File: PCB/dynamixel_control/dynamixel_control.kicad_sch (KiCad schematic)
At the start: 34 parts, among them J1 12V, J2 RS232, J3 5V, J4 3.3V, J5 I2C, Q1 SSM3J372R, SW1 LIMIT_SWITCH, U1 R-78E5.0-0.5, U2 SN74AHC1G14, U3 LM810M3-4.63, U4 Teensy_4.0, U5 MAX3221E, U6 ICM-40627

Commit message: Fix issues. Add schematic files.
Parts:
- added C6: 10nF/25V, Capacitor_SMD:C_0805_2012Metric, symbol Device:C
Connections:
- net +3.3V: now also C6.1
- net GND: now also C6.2
- net IMU_INT1: now also U4.14 (14/A0/TX3/SPDIF_OUT/PWM); no longer U4.13 (13/LED/SCK/PWM)
- net IMU_INT2: now also U4.15 (15/A1/RX3/SPDIF_IN/PWM); no longer U4.16 (16/A2/RX4/SCL1)
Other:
- note added: "I2C Address 1101000: R9=NI, R10=0 1101001: R9=0, R10=NI NI: Not Installed"
- title: (none) -> Dynamixel Control
- moved on the sheet: C12, C13

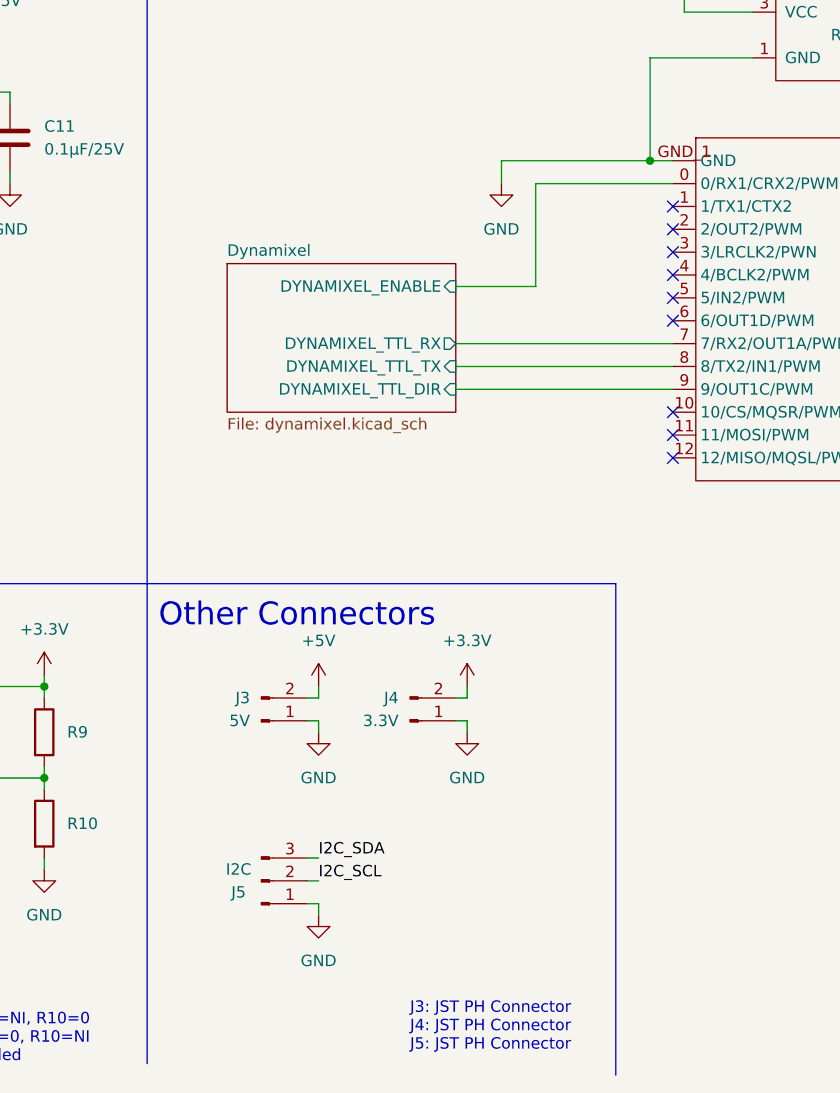
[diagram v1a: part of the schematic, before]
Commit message: Add Debug UART connector to dynamixel_control.
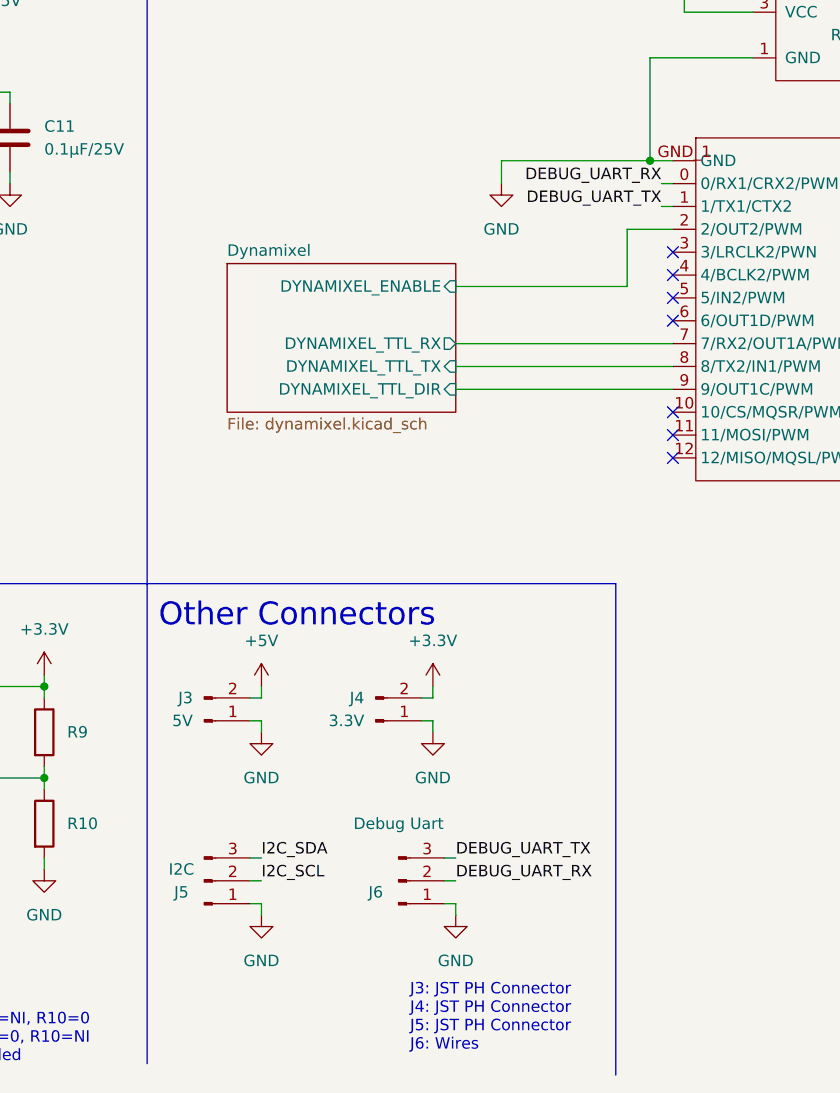
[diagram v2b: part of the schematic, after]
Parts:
- added J6: Debug Uart, Connector_PinHeader_1.00mm:PinHeader_1x03_P1.00mm_Vertical, symbol Connector:Conn_01x03_Male
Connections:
- net Dynamixel/DYNAMIXEL_ENABLE: now also U4.2 (2/OUT2/PWM); no longer U4.0 (0/RX1/CRX2/PWM)
- net GND: now also J6.1 (Pin_1)
- net DEBUG_UART_TX: now reaches U4.1 (1/TX1/CTX2)
- net DEBUG_UART_TX: now also J6.3 (Pin_3)
- new net DEBUG_UART_RX: J6.2 (Pin_2), U4.0 (0/RX1/CRX2/PWM)
- no-connect marks 13 -> 11
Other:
- note added: "J3: JST PH Connector J4: JST PH Connector J5: JST PH Connector J6: Wires"
- note removed: "J3: JST PH Connector J4: JST PH Connector J5: JST PH Connector"
- moved on the sheet: J3, J4, J5

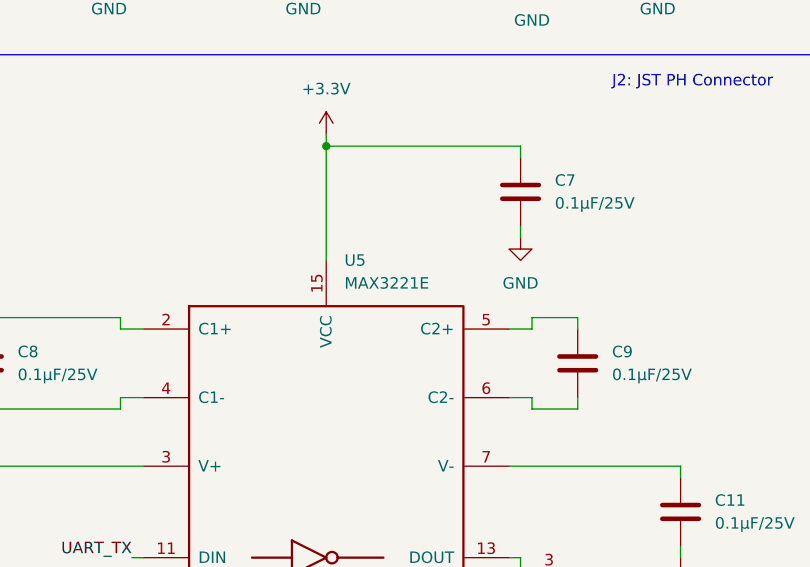
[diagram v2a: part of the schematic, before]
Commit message: Change MAX3221E by SN65C3221E.
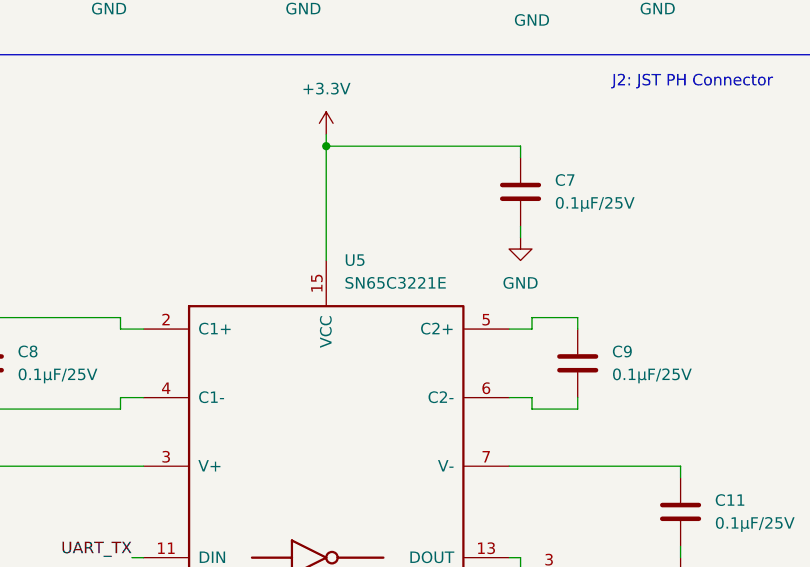
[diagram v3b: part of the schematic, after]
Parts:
- removed U5: MAX3221E, Package_SO:TSSOP-16_4.4x5mm_P0.65mm, symbol t-top:MAX3221E
- added U5: SN65C3221E, Package_SO:TSSOP-16_4.4x5mm_P0.65mm, symbol t-top:SN65C3221E
- J6: footprint Connector_PinHeader_1.00mm:PinHeader_1x03_P1.00mm_Vertical -> Connector_PinHeader_1.27mm:PinHeader_1x03_P1.27mm_Vertical
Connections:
- net +3.3V: now also U5.12 (FORCEON), U5.15 (VCC), U5.16 (~{FORCEOFF})
- net GND: now also U5.1 (~{EN}), U5.14 (GND)
- net UART_RX: now also U5.9 (ROUT)
- net UART_TX: now also U5.11 (DIN)
- net ~{RS232_INVALID}: now also U5.10 (~{INVALID})
- net at C8.1: now also U5.2 (C1+)
- net at C8.2: now also U5.4 (C1-)
- net at J2.2 (Pin_2): now also U5.8 (RIN)
- net at J2.3 (Pin_3): now also U5.13 (DOUT)
- net at C11.1: now also U5.7 (V-)
- net at C10.1: now also U5.3 (V+)
- net at C9.1: now also U5.5 (C2+)
- net at C9.2: now also U5.6 (C2-)
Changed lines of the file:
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@@
     (property "Reference" "J6" (id 0) (at 149.86 177.8 0))
     (property "Value" "Debug Uart" (id 1) (at 152.4 170.18 0))
-    (property "Footprint" "Connector_PinHeader_1.00mm:PinHeader_1x03_P1.00mm_Vertical" (id 2) (at 152.4 176.53 0)
+    (property "Footprint" "Connector_PinHeader_1.27mm:PinHeader_1x03_P1.27mm_Vertical" (id 2) (at 152.4 176.53 0)
       (effects (font (size 1.27 1.27)) hide)
     )
@@
     (pin "3")
   )
-  (symbol (lib_id "power:GND") (at 179.07 50.8 0) (unit 1)
-    (in_bom yes) (on_board yes) (fields_autoplaced)
-    (property "Reference" "#PWR0135" (id 0) (at 179.07 57.15 0)
-      (effects (font (size 1.27 1.27)) hide)
-    )
-    (property "Value" "GND" (id 1) (at 179.07 55.88 0))
-    (property "Footprint" "" (id 2) (at 179.07 50.8 0)
-      (effects (font (size 1.27 1.27)) hide)
-    )
-    (property "Datasheet" "" (id 3) (at 179.07 50.8 0)
-      (effects (font (size 1.27 1.27)) hide)
-    )
-    (pin "1")
-  )
-  (symbol (lib_id "Device:C") (at 109.22 93.98 0) (unit 1)
-    (in_bom yes) (on_board yes) (fields_autoplaced)
-    (property "Reference" "C11" (id 0) (at 113.03 92.7099 0)
-      (effects (font (size 1.27 1.27)) (justify left))
-    )
-    (property "Value" "0.1µF/25V" (id 1) (at 113.03 95.2499 0)
-      (effects (font (size 1.27 1.27)) (justify left))
-    )
-    (property "Footprint" "Capacitor_SMD:C_0805_2012Metric" (id 2) (at 110.1852 97.79 0)
-      (effects (font (size 1.27 1.27)) hide)
-    )
-    (property "Datasheet" "~" (id 3) (at 109.22 93.98 0)
-      (effects (font (size 1.27 1.27)) hide)
-    )
-    (pin "1")
-    (pin "2")
-  )
-  (symbol (lib_id "Connector:Conn_01x03_Male") (at 130.81 176.53 0) (mirror x) (unit 1)
-    (in_bom yes) (on_board yes)
-    (property "Reference" "J5" (id 0) (at 128.27 177.8 0))
-    (property "Value" "I2C" (id 1) (at 128.27 175.26 0))
-    (property "Footprint" "Connector_JST:JST_PH_B3B-PH-K_1x03_P2.00mm_Vertical" (id 2) (at 130.81 176.53 0)
-      (effects (font (size 1.27 1.27)) hide)
-    )
-    (property "Datasheet" "~" (id 3) (at 130.81 176.53 0)
-      (effects (font (size 1.27 1.27)) hide)
-    )
-    (pin "1")
-    (pin "2")
-    (pin "3")
-  )
-  (symbol (lib_id "power:GND") (at 67.31 33.02 0) (unit 1)
-    (in_bom yes) (on_board yes) (fields_autoplaced)
-    (property "Reference" "#PWR0113" (id 0) (at 67.31 39.37 0)
-      (effects (font (size 1.27 1.27)) hide)
-    )
-    (property "Value" "GND" (id 1) (at 67.31 38.1 0))
-    (property "Footprint" "" (id 2) (at 67.31 33.02 0)
-      (effects (font (size 1.27 1.27)) hide)
-    )
-    (property "Datasheet" "" (id 3) (at 67.31 33.02 0)
-      (effects (font (size 1.27 1.27)) hide)
-    )
-    (pin "1")
-  )
-  (symbol (lib_id "Switch:SW_SPST") (at 132.08 43.18 90) (unit 1)
-    (in_bom yes) (on_board yes)
-    (property "Reference" "SW1" (id 0) (at 133.35 41.9099 90)
-      (effects (font (size 1.27 1.27)) (justify right))
-    )
-    (property "Value" "LIMIT_SWITCH" (id 1) (at 133.35 44.45 90)
-      (effects (font (size 1.27 1.27)) (justify right))
-    )
-    (property "Footprint" "Connector_JST:JST_PH_B2B-PH-K_1x02_P2.00mm_Vertical" (id 2) (at 132.08 43.18 0)
-      (effects (font (size 1.27 1.27)) hide)
-    )
-    (property "Datasheet" "~" (id 3) (at 132.08 43.18 0)
-      (effects (font (size 1.27 1.27)) hide)
-    )
-    (pin "1")
-    (pin "2")
-  )
-  (symbol (lib_id "Device:C") (at 16.51 93.98 0) (unit 1)
-    (in_bom yes) (on_board yes) (fields_autoplaced)
-    (property "Reference" "C10" (id 0) (at 20.32 92.7099 0)
-      (effects (font (size 1.27 1.27)) (justify left))
-    )
-    (property "Value" "0.1µF/25V" (id 1) (at 20.32 95.2499 0)
-      (effects (font (size 1.27 1.27)) (justify left))
-    )
-    (property "Footprint" "Capacitor_SMD:C_0805_2012Metric" (id 2) (at 17.4752 97.79 0)
-      (effects (font (size 1.27 1.27)) hide)
-    )
-    (property "Datasheet" "~" (id 3) (at 16.51 93.98 0)
-      (effects (font (size 1.27 1.27)) hide)
-    )
-    (pin "1")
-    (pin "2")
-  )
-  (symbol (lib_id "t-top:MAX3221E") (at 69.85 96.52 0) (unit 1)
+  (symbol (lib_id "t-top:SN65C3221E") (at 69.85 96.52 0) (unit 1)
     (in_bom yes) (on_board yes) (fields_autoplaced)
     (property "Reference" "U5" (id 0) (at 71.8694 66.04 0)
       (effects (font (size 1.27 1.27)) (justify left))
     )
-    (property "Value" "MAX3221E" (id 1) (at 71.8694 68.58 0)
+    (property "Value" "SN65C3221E" (id 1) (at 71.8694 68.58 0)
       (effects (font (size 1.27 1.27)) (justify left))
     )
@@
     (pin "8")
     (pin "9")
+  )
+  (symbol (lib_id "power:GND") (at 179.07 50.8 0) (unit 1)
+    (in_bom yes) (on_board yes) (fields_autoplaced)
+    (property "Reference" "#PWR0135" (id 0) (at 179.07 57.15 0)
+      (effects (font (size 1.27 1.27)) hide)
+    )
+    (property "Value" "GND" (id 1) (at 179.07 55.88 0))
+    (property "Footprint" "" (id 2) (at 179.07 50.8 0)
+      (effects (font (size 1.27 1.27)) hide)
+    )
+    (property "Datasheet" "" (id 3) (at 179.07 50.8 0)
+      (effects (font (size 1.27 1.27)) hide)
+    )
+    (pin "1")
+  )
+  (symbol (lib_id "Device:C") (at 109.22 93.98 0) (unit 1)
+    (in_bom yes) (on_board yes) (fields_autoplaced)
+    (property "Reference" "C11" (id 0) (at 113.03 92.7099 0)
+      (effects (font (size 1.27 1.27)) (justify left))
+    )
+    (property "Value" "0.1µF/25V" (id 1) (at 113.03 95.2499 0)
+      (effects (font (size 1.27 1.27)) (justify left))
+    )
+    (property "Footprint" "Capacitor_SMD:C_0805_2012Metric" (id 2) (at 110.1852 97.79 0)
+      (effects (font (size 1.27 1.27)) hide)
+    )
+    (property "Datasheet" "~" (id 3) (at 109.22 93.98 0)
+      (effects (font (size 1.27 1.27)) hide)
+    )
+    (pin "1")
+    (pin "2")
+  )
+  (symbol (lib_id "Connector:Conn_01x03_Male") (at 130.81 176.53 0) (mirror x) (unit 1)
+    (in_bom yes) (on_board yes)
+    (property "Reference" "J5" (id 0) (at 128.27 177.8 0))
+    (property "Value" "I2C" (id 1) (at 128.27 175.26 0))
+    (property "Footprint" "Connector_JST:JST_PH_B3B-PH-K_1x03_P2.00mm_Vertical" (id 2) (at 130.81 176.53 0)
+      (effects (font (size 1.27 1.27)) hide)
+    )
+    (property "Datasheet" "~" (id 3) (at 130.81 176.53 0)
+      (effects (font (size 1.27 1.27)) hide)
+    )
+    (pin "1")
+    (pin "2")
+    (pin "3")
+  )
+  (symbol (lib_id "power:GND") (at 67.31 33.02 0) (unit 1)
+    (in_bom yes) (on_board yes) (fields_autoplaced)
+    (property "Reference" "#PWR0113" (id 0) (at 67.31 39.37 0)
+      (effects (font (size 1.27 1.27)) hide)
+    )
+    (property "Value" "GND" (id 1) (at 67.31 38.1 0))
+    (property "Footprint" "" (id 2) (at 67.31 33.02 0)
+      (effects (font (size 1.27 1.27)) hide)
+    )
+    (property "Datasheet" "" (id 3) (at 67.31 33.02 0)
+      (effects (font (size 1.27 1.27)) hide)
+    )
+    (pin "1")
+  )
+  (symbol (lib_id "Switch:SW_SPST") (at 132.08 43.18 90) (unit 1)
+    (in_bom yes) (on_board yes)
+    (property "Reference" "SW1" (id 0) (at 133.35 41.9099 90)
+      (effects (font (size 1.27 1.27)) (justify right))
+    )
+    (property "Value" "LIMIT_SWITCH" (id 1) (at 133.35 44.45 90)
+      (effects (font (size 1.27 1.27)) (justify right))
+    )
+    (property "Footprint" "Connector_JST:JST_PH_B2B-PH-K_1x02_P2.00mm_Vertical" (id 2) (at 132.08 43.18 0)
+      (effects (font (size 1.27 1.27)) hide)
+    )
+    (property "Datasheet" "~" (id 3) (at 132.08 43.18 0)
+      (effects (font (size 1.27 1.27)) hide)
+    )
+    (pin "1")
+    (pin "2")
+  )
+  (symbol (lib_id "Device:C") (at 16.51 93.98 0) (unit 1)
+    (in_bom yes) (on_board yes) (fields_autoplaced)
+    (property "Reference" "C10" (id 0) (at 20.32 92.7099 0)
+      (effects (font (size 1.27 1.27)) (justify left))
+    )
+    (property "Value" "0.1µF/25V" (id 1) (at 20.32 95.2499 0)
+      (effects (font (size 1.27 1.27)) (justify left))
+    )
+    (property "Footprint" "Capacitor_SMD:C_0805_2012Metric" (id 2) (at 17.4752 97.79 0)
+      (effects (font (size 1.27 1.27)) hide)
+    )
+    (property "Datasheet" "~" (id 3) (at 16.51 93.98 0)
+      (effects (font (size 1.27 1.27)) hide)
+    )
+    (pin "1")
+    (pin "2")
   )
   (symbol (lib_id "power:GND") (at 52.07 185.42 0) (unit 1)
@@
     )
     (path "/10b4d070-9fcb-4662-96ad-09ebfc6675de"
-      (reference "J6") (unit 1) (value "Debug Uart") (footprint "Connector_PinHeader_1.00mm:PinHeader_1x03_P1.00mm_Vertical")
+      (reference "J6") (unit 1) (value "Debug Uart") (footprint "Connector_PinHeader_1.27mm:PinHeader_1x03_P1.27mm_Vertical")
     )
     (path "/d35e0dd5-65a6-42a8-88be-82a5f6d1ca91/a88625c8-ea46-49fd-853f-e88ba2b2fda3"
@@
       (reference "U4") (unit 1) (value "Teensy_4.0") (footprint "t-top:Teensy_4.0")
     )
-    (path "/c0ae8657-d6e0-4e58-ba13-3af268c90837"
-      (reference "U5") (unit 1) (value "MAX3221E") (footprint "Package_SO:TSSOP-16_4.4x5mm_P0.65mm")
+    (path "/abc9de71-4b88-443a-8b78-70ae89426f7f"
+      (reference "U5") (unit 1) (value "SN65C3221E") (footprint "Package_SO:TSSOP-16_4.4x5mm_P0.65mm")
     )
     (path "/7d19cc23-7b93-4a41-844a-abd34722bd1b"

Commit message: Fix PCBs.
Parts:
- removed J3: 5V, Connector_JST:JST_PH_B2B-PH-K_1x02_P2.00mm_Vertical, symbol Connector:Conn_01x02_Male
- removed J4: 3.3V, Connector_JST:JST_PH_B2B-PH-K_1x02_P2.00mm_Vertical, symbol Connector:Conn_01x02_Male
- removed J5: I2C, Connector_JST:JST_PH_B3B-PH-K_1x03_P2.00mm_Vertical, symbol Connector:Conn_01x03_Male
- added C14: 10µF/25V, Capacitor_SMD:C_0805_2012Metric, symbol Device:C
- added L2: 12µH (RLS-126), Inductor_SMD:L_1812_4532Metric, symbol Device:L
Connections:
- net +5V: now also C14.1, L2.2; no longer C3.1, U1.3 (VOUT)
- net GND: now also C14.2
- new net: C3.1, L2.1, U1.3 (VOUT)
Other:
- note added: "Debug UART"
- note added: "J6: Wires"
- note removed: "J3: JST PH Connector J4: JST PH Connector J5: JST PH Connector J6: Wires"
- note removed: "Other Connectors"
- moved on the sheet: C1, C2, C3, J1, J6, L1, U1

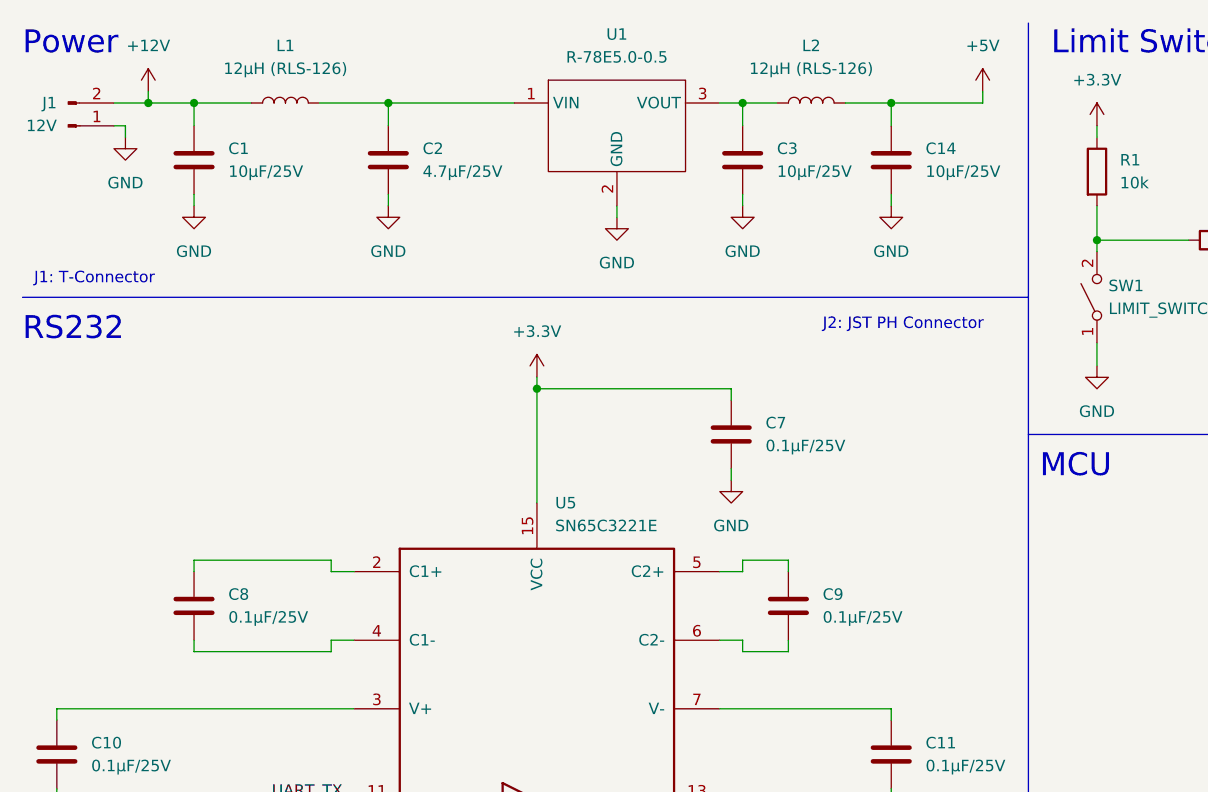
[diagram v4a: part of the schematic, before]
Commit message: Add a PI filter to buck_boost. Fix ringing for other PI filters.
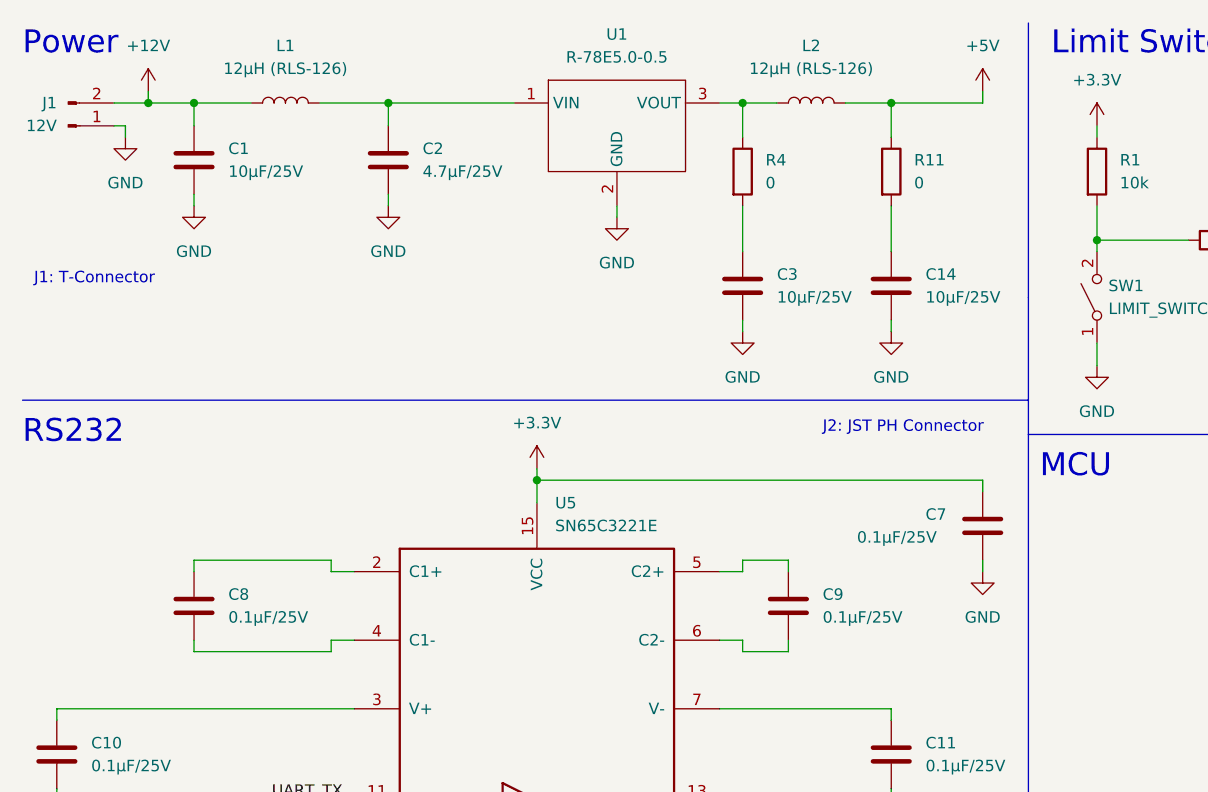
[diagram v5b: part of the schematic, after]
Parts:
- added R11, R4: 0, Resistor_SMD:R_0805_2012Metric, symbol Device:R
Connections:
- net +5V: now also R11.1; no longer C14.1
- net at L2.1, U1.3 (VOUT): now also R4.1; no longer C3.1
- new net: C14.1, R11.2
- new net: C3.1, R4.2
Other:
- moved on the sheet: C14, C3, C7
